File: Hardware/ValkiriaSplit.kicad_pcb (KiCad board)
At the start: 4 copper layers, 350 x 195 mm, 306 parts, among them J1 BAT, J2 TagConnect, J3 0.96_TFT_MODULE, J4 BAT, J5 TagConnect, J6 0.96_TFT_MODULE, Q1 AO3401A, Q2 AO3401A, Q3 AO3401A, Q4 AO3401A, SW1 MSK12C02, SW10 PG1350, SW11 PG1350, SW12 PG1350, SW13 PG1350, SW14 PG1350, SW15 PG1350, SW16 PG1350, SW17 PG1350, SW18 PG1350, SW19 PG1350, SW2 MSK12C02, SW20 PG1350, SW21 PG1350, SW22 PG1350, SW23 PG1350, SW24 PG1350, SW25 PG1350, SW26 PG1350, SW27 PG1350, SW28 PG1350, SW29 PG1350, SW3 PG1350, SW30 PG1350, SW31 PG1350, SW32 ENCODER, SW33 PG1350, SW34 PG1350, SW35 PG1350, SW36 PG1350, SW37 PG1350, SW38 PG1350, SW39 PG1350, SW4 PG1350, SW40 PG1350, SW41 PG1350, SW42 PG1350, SW43 PG1350, SW44 PG1350, SW45 PG1350, SW46 PG1350, SW47 PG1350, SW48 PG1350, SW49 PG1350, SW5 PG1350, SW50 PG1350, SW51 PG1350, SW52 PG1350, SW53 PG1350, SW54 PG1350, SW55 PG1350, SW56 PG1350, SW57 PG1350, SW58 PG1350, SW59 PG1350, SW6 PG1350, SW60 PG1350, SW61 PG1350, SW62 ENCODER, SW7 PG1350, SW8 PG1350, SW9 PG1350, U1 TPS61040DBV, U2 XIAO-NRF52840-PLUS, U3 TPS61040DBV, U4 XIAO-NRF52840-PLUS

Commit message: Key matrix and edges
Defined the key matrix locations and the board edges.
Next step: start routing and verify the buck converter layout.
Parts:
- added C75: 100n, Capacitor_SMD:C_0603_1608Metric, F.Cu at (259.0, 216.8)
- added C76: 100n, Capacitor_SMD:C_0603_1608Metric, F.Cu at (259.0, 219.3)
- added D125: SK6812MINI-E, Custom_Parts:LED_SK6812MINI-E_3.2x2.8mm_P1.5mm_ReverseMount, B.Cu at (313.7, 96.4)
- added D126: SK6812MINI-E, Custom_Parts:LED_SK6812MINI-E_3.2x2.8mm_P1.5mm_ReverseMount, B.Cu at (275.6, 127.3)
- added R23: 10K, Resistor_SMD:R_0603_1608Metric, F.Cu at (308.4, 230.8)
- added R24: 22, Resistor_SMD:R_0603_1608Metric, F.Cu at (308.4, 233.3)
- added R25: 0, Resistor_SMD:R_0603_1608Metric, F.Cu at (113.0, 220.9)
- added R26: 0, Resistor_SMD:R_0603_1608Metric, F.Cu at (113.0, 223.4)
- added R27: 0, Resistor_SMD:R_0603_1608Metric, F.Cu at (259.0, 221.8)
- added R28: 0, Resistor_SMD:R_0603_1608Metric, F.Cu at (259.0, 224.3)
- added SW63: PG1350, Custom_Parts:PG1350_1.00u_PCB, F.Cu at (330.2, 125.5)
- added SW64: PG1350, Custom_Parts:PG1350_1.00u_PCB, F.Cu at (330.2, 144.6)
- added SW65: PG1350, Custom_Parts:PG1350_1.00u_PCB, F.Cu at (330.2, 163.6)
- added SW66: ENCODER, Custom_Parts:ALPS_EC11J_ENCODER, F.Cu at (216.4, 134.0)
- C13, FID1, FID2, FID3, FID4: moved to B.Cu
- C42, C73, C74: value 100n -> 1u; moved to B.Cu
- C44: value 1u -> 100n; moved to F.Cu
- D103, D104, D119, D120, D17, D26, D35, D44, D47, D60, D76, D77, D85, D86, D94, D95: value SK6812MINI-E -> 1N4148WT; footprint Custom_Parts:LED_SK6812MINI-E_3.2x2.8mm_P1.5mm_ReverseMount -> Diode_SMD:D_SOD-523
- D114, D115, D12, D21, D30, D39, D52, D55, D71, D72, D80, D81, D89, D90, D98, D99: value 1N4148WT -> SK6812MINI-E; footprint Diode_SMD:D_SOD-523 -> Custom_Parts:LED_SK6812MINI-E_3.2x2.8mm_P1.5mm_ReverseMount
- J3, J6: footprint Custom_Parts:Jushuo_AFC07-S06FCA-00_1x8-1MP_P0.50_Horizontal -> Custom_Parts:0.96_TFT_MODULE; moved to B.Cu
- L1, L2: footprint Custom_Parts:VLCF4020 -> Custom_Parts:VLCF4020_MIRROR
- R1: value 500 -> 100K
- R10: value 500 -> 10K
- R11: value 100K -> 10K
- R12: value 10K -> 22
- R13: value 470K -> 100K
- R14: value 150K -> 500
- R15: value 100 -> 10K
- R16: value 10K -> 470K
- R17: value 10K -> 150K
- R18: value 22 -> 0
- R2: value 100K -> 500
- R21: value 0 -> 100
- R22: value 0 -> 10K
- R6: value 100 -> 0
- R7, R8: value 10K -> 0
- R9: value 22 -> 100
- SW2: value MSK12C02 -> RESET; footprint Custom_Parts:MSK12C02 -> Button_Switch_SMD:SW_SPST_TS-1088-xR020
- SW3: value PG1350 -> MSK12C02; footprint Custom_Parts:PG1350_1.00u_PCB -> Custom_Parts:MSK12C02
- SW32, SW62: value ENCODER -> PG1350; footprint Custom_Parts:ALPS_EC11J_ENCODER -> Custom_Parts:PG1350_1.00u_PCB
- SW35: value PG1350 -> ENCODER; footprint Custom_Parts:PG1350_1.00u_PCB -> Custom_Parts:ALPS_EC11J_ENCODER
- SW4: value PG1350 -> RESET; footprint Custom_Parts:PG1350_1.00u_PCB -> Button_Switch_SMD:SW_SPST_TS-1088-xR020
- moved R10 381.5 mm to (86.1, 231.5)
- moved R11 381.5 mm to (86.1, 234.0)
- moved R12 381.5 mm to (86.1, 236.5)
- moved SW2 332.1 mm to (145.4, 233.9)
- moved R20 316.8 mm to (288.5, 221.0)
- moved R19 316.8 mm to (288.5, 218.5)
- moved SW34 306.2 mm to (64.8, 163.6), turned to 180 degrees
- moved R16 271.0 mm to (208.5, 239.0)
- moved R17 267.2 mm to (212.0, 240.0)
- moved C9 263.4 mm to (208.5, 241.0)
- moved SW4 260.9 mm to (288.1, 234.1)
- moved D1 258.5 mm to (193.5, 234.3)
- moved R15 256.5 mm to (215.5, 240.0), turned to 180 degrees
- moved Q1 256.2 mm to (193.5, 237.8), turned to -90 degrees
- moved C44 255.1 mm to (113.0, 218.4), turned to 0 degrees
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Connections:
- net /Control_Left/VFBL renamed /Control_Left/VFB
- net /Control_Left/VSWL renamed /Control_Left/VSW
- net /Control_Right/VSWR renamed /Control_Right/VSW
- C42 pad 1: /Matrix_Left/ENC_CC -> 5VL
- C43 pad 1: /Matrix_Left/ENC_CW -> /Matrix_Left/ENC_CC
- C44 pad 1: 5VR -> /Matrix_Left/ENC_CW
- C73 pad 1: /Matrix_Right/ENC_CC -> 5VR
- C74 pad 1: /Matrix_Right/ENC_CW -> 5VR
- C9 pad 2: /Control_Right/VFBR -> /Control_Right/VFB
- D100 pad 1: ROW3_R -> ROW1_R
- D101 pad 1: ROW4_R -> ROW2_R
- D102 pad 1: ROW5_R -> ROW3_R
- D103 pad 1: GND -> ROW4_R
- D103 pad 2: Net-(D103-DIN) -> Net-(D103-A)
- D104 pad 1: GND -> ROW5_R
- D104 pad 2: Net-(D104-DIN) -> Net-(D104-A)
- D112 pad 4: Net-(D103-DIN) -> Net-(D112-DOUT)
- D113 pad 4: Net-(D104-DIN) -> Net-(D113-DOUT)
- D114 pad 1: ROW1_R -> GND
- D114 pad 2: Net-(D114-A) -> Net-(D114-DIN)
- D115 pad 1: ROW2_R -> GND
- D115 pad 2: Net-(D115-A) -> Net-(D115-DIN)
- D116 pad 1: ROW3_R -> ROW1_R
- D117 pad 1: ROW4_R -> ROW2_R
- D118 pad 1: ROW5_R -> ROW3_R
- D118 pad 2: /Matrix_Right/ENC_SW -> Net-(D118-A)
- D119 pad 1: GND -> ROW4_R
- D119 pad 2: Net-(D105-DOUT) -> Net-(D119-A)
- D12 pad 1: ROW1_L -> GND
- D12 pad 2: Net-(D12-A) -> Net-(D12-DIN)
- D120 pad 1: GND -> ROW5_R
- D120 pad 2: Net-(D106-DOUT) -> /Matrix_Right/ENC_SW
- D121 pad 2: Net-(D121-DIN) -> Net-(D112-DOUT)
- D121 pad 4: Net-(D112-DIN) -> Net-(D121-DOUT)
- D122 pad 2: Net-(D122-DIN) -> Net-(D113-DOUT)
- D122 pad 4: Net-(D113-DIN) -> Net-(D122-DOUT)
- D123 pad 2: Net-(D119-DOUT) -> Net-(D123-DIN)
- D123 pad 4: Net-(D121-DIN) -> Net-(D114-DIN)
- D124 pad 2: Net-(D120-DOUT) -> Net-(D124-DIN)
- D124 pad 4: Net-(D122-DIN) -> Net-(D115-DIN)
- D13 pad 1: ROW2_L -> ROW1_L
- D14 pad 1: ROW3_L -> ROW2_L
- D15 pad 1: ROW4_L -> ROW3_L
- D16 pad 1: ROW5_L -> ROW4_L
- D17 pad 1: GND -> ROW5_L
- D17 pad 2: Net-(D17-DIN) -> Net-(D17-A)
- D19 pad 2: Net-(D10-DOUT) -> Net-(D19-DIN)
- D19 pad 4: Net-(D19-DOUT) -> Net-(D10-DIN)
- D21 pad 1: ROW1_L -> GND
- D21 pad 2: Net-(D21-A) -> Net-(D12-DOUT)
- D22 pad 1: ROW2_L -> ROW1_L
- D23 pad 1: ROW3_L -> ROW2_L
- D24 pad 1: ROW4_L -> ROW3_L
- D25 pad 1: ROW5_L -> ROW4_L
- D26 pad 1: GND -> ROW5_L
- D26 pad 2: Net-(D26-DIN) -> Net-(D26-A)
- D28 pad 2: Net-(D19-DOUT) -> Net-(D28-DIN)
- D28 pad 4: Net-(D28-DOUT) -> Net-(D19-DIN)
- D30 pad 1: ROW1_L -> GND
- D30 pad 2: Net-(D30-A) -> Net-(D21-DOUT)
- D31 pad 1: ROW2_L -> ROW1_L
- D32 pad 1: ROW3_L -> ROW2_L
- D33 pad 1: ROW4_L -> ROW3_L
- D34 pad 1: ROW5_L -> ROW4_L
- D35 pad 1: GND -> ROW5_L
- D35 pad 2: Net-(D35-DIN) -> Net-(D35-A)
- D37 pad 2: Net-(D28-DOUT) -> Net-(D37-DIN)
- D37 pad 4: Net-(D37-DOUT) -> Net-(D28-DIN)
- D39 pad 1: ROW1_L -> GND
- D39 pad 2: Net-(D39-A) -> Net-(D30-DOUT)
- D40 pad 1: ROW2_L -> ROW1_L
- D41 pad 1: ROW3_L -> ROW2_L
- D42 pad 1: ROW4_L -> ROW3_L
- D43 pad 1: ROW5_L -> ROW4_L
- D44 pad 1: GND -> ROW5_L
- D44 pad 2: Net-(D44-DIN) -> Net-(D44-A)
- D46 pad 2: Net-(D37-DOUT) -> Net-(D46-DIN)
- D46 pad 4: Net-(D46-DOUT) -> Net-(D37-DIN)
- D47 pad 1: GND -> ROW1_L
- D47 pad 2: Net-(D38-DOUT) -> Net-(D47-A)
- D48 pad 1: ROW1_L -> ROW2_L
- D49 pad 1: ROW2_L -> ROW3_L
- D50 pad 1: ROW3_L -> ROW4_L
- D51 pad 1: ROW4_L -> ROW5_L
- D52 pad 1: ROW5_L -> GND
- D52 pad 2: Net-(D52-A) -> Net-(D38-DOUT)
- D53 pad 2: Net-(D53-DIN) -> Net-(D39-DOUT)
- D53 pad 4: Net-(D44-DIN) -> Net-(D53-DOUT)
- D55 pad 1: ROW1_L -> GND
- D55 pad 2: Net-(D55-A) -> Net-(D55-DIN)
- D56 pad 1: ROW2_L -> ROW1_L
- D57 pad 1: ROW3_L -> ROW2_L
- D58 pad 1: ROW4_L -> ROW3_L
- D59 pad 1: ROW5_L -> ROW4_L
- D59 pad 2: /Matrix_Left/ENC_SW -> Net-(D59-A)
- D6 pad 1: 3V3L -> 3V3R
- D60 pad 1: GND -> ROW5_L
- D60 pad 2: Net-(D46-DOUT) -> /Matrix_Left/ENC_SW
- D61 pad 2: Net-(D47-DOUT) -> Net-(D52-DOUT)
- D62 pad 2: Net-(D62-DIN) -> Net-(D53-DOUT)
- D62 pad 4: Net-(D53-DIN) -> Net-(D62-DOUT)
- D64 pad 2: Net-(D60-DOUT) -> Net-(D64-DIN)
- D64 pad 4: Net-(D62-DIN) -> Net-(D55-DIN)
- D66 pad 2: LED_DATA_R -> Net-(D62-DOUT)
- D66 pad 3: 5VR -> 5VL
- D66 pad 4: Net-(D66-DOUT) -> Net-(D64-DIN)
- D67 pad 4: Net-(D67-DOUT) -> unconnected-(D67-DOUT-Pad4)
- D68 pad 2: Net-(D68-DIN) -> LED_DATA_R
- D68 pad 4: unconnected-(D68-DOUT-Pad4) -> Net-(D68-DOUT)
- D69 pad 2: Net-(D66-DOUT) -> Net-(D69-DIN)
- D7 pad 2: LED_DATA_L -> Net-(D10-DOUT)
- D7 pad 4: Net-(D10-DIN) -> unconnected-(D7-DOUT-Pad4)
- D70 pad 2: Net-(D67-DOUT) -> Net-(D70-DIN)
- D70 pad 4: Net-(D70-DOUT) -> Net-(D67-DIN)
- D71 pad 1: ROW1_R -> GND
- D71 pad 2: Net-(D71-A) -> Net-(D68-DOUT)
- D72 pad 1: ROW2_R -> GND
- D72 pad 2: Net-(D72-A) -> Net-(D69-DOUT)
- D73 pad 1: ROW3_R -> ROW1_R
- D74 pad 1: ROW4_R -> ROW2_R
- D75 pad 1: ROW5_R -> ROW3_R
- D76 pad 1: GND -> ROW4_R
- D76 pad 2: Net-(D76-DIN) -> Net-(D76-A)
- D77 pad 1: GND -> ROW5_R
- D77 pad 2: Net-(D77-DIN) -> Net-(D77-A)
- D78 pad 2: Net-(D69-DOUT) -> Net-(D78-DIN)
- D78 pad 4: Net-(D78-DOUT) -> Net-(D69-DIN)
- D79 pad 2: Net-(D70-DOUT) -> Net-(D79-DIN)
- D79 pad 4: Net-(D79-DOUT) -> Net-(D70-DIN)
- D8 pad 2: Net-(D17-DOUT) -> LED_DATA_L
- D80 pad 1: ROW1_R -> GND
- D80 pad 2: Net-(D80-A) -> Net-(D71-DOUT)
- D81 pad 1: ROW2_R -> GND
- D81 pad 2: Net-(D81-A) -> Net-(D72-DOUT)
- D82 pad 1: ROW3_R -> ROW1_R
- D83 pad 1: ROW4_R -> ROW2_R
- D84 pad 1: ROW5_R -> ROW3_R
- D85 pad 1: GND -> ROW4_R
- D85 pad 2: Net-(D85-DIN) -> Net-(D85-A)
- D86 pad 1: GND -> ROW5_R
- D86 pad 2: Net-(D86-DIN) -> Net-(D86-A)
- D87 pad 2: Net-(D78-DOUT) -> Net-(D87-DIN)
- D87 pad 4: Net-(D87-DOUT) -> Net-(D78-DIN)
- D88 pad 2: Net-(D79-DOUT) -> Net-(D88-DIN)
- D88 pad 4: Net-(D88-DOUT) -> Net-(D79-DIN)
- D89 pad 1: ROW1_R -> GND
- D89 pad 2: Net-(D89-A) -> Net-(D80-DOUT)
- D9 pad 4: unconnected-(D9-DOUT-Pad4) -> Net-(D12-DIN)
- D90 pad 1: ROW2_R -> GND
- D90 pad 2: Net-(D90-A) -> Net-(D81-DOUT)
- D91 pad 1: ROW3_R -> ROW1_R
- D92 pad 1: ROW4_R -> ROW2_R
- D93 pad 1: ROW5_R -> ROW3_R
- D94 pad 1: GND -> ROW4_R
- D94 pad 2: Net-(D103-DOUT) -> Net-(D94-A)
- D95 pad 1: GND -> ROW5_R
- D95 pad 2: Net-(D104-DOUT) -> Net-(D95-A)
- D96 pad 2: Net-(D87-DOUT) -> Net-(D105-DOUT)
- D96 pad 4: Net-(D105-DIN) -> Net-(D87-DIN)
- D97 pad 2: Net-(D88-DOUT) -> Net-(D106-DOUT)
- D97 pad 4: Net-(D106-DIN) -> Net-(D88-DIN)
- D98 pad 1: ROW1_R -> GND
- D98 pad 2: Net-(D98-A) -> Net-(D89-DOUT)
- D99 pad 1: ROW2_R -> GND
- D99 pad 2: Net-(D99-A) -> Net-(D90-DOUT)
- R1 pad 1: /Control_Left/LED_DATA -> VBUSL
- R1 pad 2: LED_DATA_L -> GND
- R10 pad 1: /Control_Right/LED_DATA -> 3V3L
- R10 pad 2: LED_DATA_R -> /Control_Left/LCD_RES
- R11 pad 1: VBUSR -> /Control_Left/BKLD
- R11 pad 2: GND -> /Control_Left/BKLG
- R12 pad 1: GND -> /Control_Left/BKLD
- R12 pad 2: /Control_Right/LED_EN -> /Control_Left/BKL
- R13 pad 1: 5VR -> VBUSR
- R13 pad 2: /Control_Right/VFBR -> GND
- R14 pad 1: /Control_Right/VFBR -> /Control_Right/LED_DATA
- R14 pad 2: GND -> LED_DATA_R
- R15 pad 1: /Control_Right/LCD_BKL -> GND
- R15 pad 2: /Control_Right/BKLG -> /Control_Right/LED_EN
- R16 pad 1: 3V3L -> 5VR
- R16 pad 2: /Control_Right/LCD_RES -> /Control_Right/VFB
- R17 pad 1: /Control_Right/BKLD -> /Control_Right/VFB
- R17 pad 2: /Control_Right/BKLG -> GND
- R18 pad 1: /Control_Right/BKLD -> Net-(U4-P1.15_MOSI)
- R18 pad 2: /Control_Right/BKL -> /Control_Right/LCD_MOSI
- R19 pad 1: ENC_CW_L -> Net-(U4-P1.14_MISO)
- R19 pad 2: /Matrix_Left/ENC_CW -> /Control_Right/LCD_DC
- R2 pad 1: VBUSL -> /Control_Left/LED_DATA
- R2 pad 2: GND -> LED_DATA_L
- R20 pad 1: ENC_CC_L -> Net-(U4-P1.13_SCK)
- R20 pad 2: /Matrix_Left/ENC_CC -> /Control_Right/LCD_SCK
- R21 pad 1: ENC_CW_R -> /Control_Right/LCD_BKL
- R21 pad 2: /Matrix_Right/ENC_CW -> /Control_Right/BKLG
- R22 pad 1: ENC_CC_R -> 3V3R
- R22 pad 2: /Matrix_Right/ENC_CC -> /Control_Right/LCD_RES
- R6 pad 1: /Control_Left/LCD_BKL -> Net-(U2-P1.15_MOSI)
- R6 pad 2: /Control_Left/BKLG -> /Control_Left/LCD_MOSI
- R7 pad 1: 3V3L -> Net-(U2-P1.14_MISO)
- R7 pad 2: /Control_Left/LCD_RES -> /Control_Left/LCD_DC
- R8 pad 1: /Control_Left/BKLD -> Net-(U2-P1.13_SCK)
- R8 pad 2: /Control_Left/BKLG -> /Control_Left/LCD_SCK
- R9 pad 1: /Control_Left/BKLD -> /Control_Left/LCD_BKL
- R9 pad 2: /Control_Left/BKL -> /Control_Left/BKLG
- SW10 pad 2: Net-(D23-A) -> Net-(D22-A)
- SW11 pad 2: Net-(D24-A) -> Net-(D23-A)
- SW12 pad 2: Net-(D25-A) -> Net-(D24-A)
- SW13 pad 1: COL3_L -> COL2_L
- SW13 pad 2: Net-(D30-A) -> Net-(D25-A)
- SW14 pad 1: COL3_L -> COL2_L
- SW14 pad 2: Net-(D31-A) -> Net-(D26-A)
- SW15 pad 2: Net-(D32-A) -> Net-(D31-A)
- SW16 pad 2: Net-(D33-A) -> Net-(D32-A)
- SW17 pad 2: Net-(D34-A) -> Net-(D33-A)
- SW18 pad 1: COL4_L -> COL3_L
- SW18 pad 2: Net-(D39-A) -> Net-(D34-A)
- SW19 pad 1: COL4_L -> COL3_L
- SW19 pad 2: Net-(D40-A) -> Net-(D35-A)
- SW2 pad 1: unconnected-(SW2-A-Pad1) -> /Control_Left/~{RESET}
- SW2 pad 2: /Control_Right/VBAT -> GND
- SW20 pad 2: Net-(D41-A) -> Net-(D40-A)
- SW21 pad 2: Net-(D42-A) -> Net-(D41-A)
- SW22 pad 2: Net-(D43-A) -> Net-(D42-A)
- SW23 pad 1: COL5_L -> COL4_L
- SW23 pad 2: Net-(D48-A) -> Net-(D43-A)
- SW24 pad 1: COL5_L -> COL4_L
- SW24 pad 2: Net-(D49-A) -> Net-(D44-A)
- SW25 pad 2: Net-(D50-A) -> Net-(D47-A)
- SW26 pad 2: Net-(D51-A) -> Net-(D48-A)
- SW27 pad 2: Net-(D52-A) -> Net-(D49-A)
- SW28 pad 1: COL6_L -> COL5_L
- SW28 pad 2: Net-(D55-A) -> Net-(D50-A)
- SW29 pad 1: COL6_L -> COL5_L
- SW29 pad 2: Net-(D56-A) -> Net-(D51-A)
- SW3 pad 1: COL1_L -> unconnected-(SW3-A-Pad1)
- SW3 pad 2: Net-(D12-A) -> /Control_Right/VBAT
- SW30 pad 2: Net-(D57-A) -> Net-(D56-A)
- SW31 pad 2: Net-(D58-A) -> Net-(D57-A)
- SW33 pad 1: COL1_R -> COL6_L
- SW33 pad 2: Net-(D71-A) -> Net-(D59-A)
- SW34 pad 1: COL1_R -> COL6_L
- SW34 pad 2: Net-(D72-A) -> /Matrix_Left/ENC_SW
- SW36 pad 2: Net-(D74-A) -> Net-(D73-A)
- SW37 pad 2: Net-(D75-A) -> Net-(D74-A)
- SW38 pad 1: COL2_R -> COL1_R
- SW38 pad 2: Net-(D80-A) -> Net-(D75-A)
- SW39 pad 1: COL2_R -> COL1_R
- SW39 pad 2: Net-(D81-A) -> Net-(D76-A)
- SW4 pad 1: COL1_L -> /Control_Right/~{RESET}
- SW4 pad 2: Net-(D13-A) -> GND
- SW40 pad 1: COL2_R -> COL1_R
- SW40 pad 2: Net-(D82-A) -> Net-(D77-A)
- SW41 pad 2: Net-(D83-A) -> Net-(D82-A)
- SW42 pad 2: Net-(D84-A) -> Net-(D83-A)
- SW43 pad 1: COL3_R -> COL2_R
- SW43 pad 2: Net-(D89-A) -> Net-(D84-A)
- SW44 pad 1: COL3_R -> COL2_R
- SW44 pad 2: Net-(D90-A) -> Net-(D85-A)
- SW45 pad 1: COL3_R -> COL2_R
- SW45 pad 2: Net-(D91-A) -> Net-(D86-A)
- SW46 pad 2: Net-(D92-A) -> Net-(D91-A)
- SW47 pad 2: Net-(D93-A) -> Net-(D92-A)
- SW48 pad 1: COL4_R -> COL3_R
- SW48 pad 2: Net-(D98-A) -> Net-(D93-A)
- SW49 pad 1: COL4_R -> COL3_R
- SW49 pad 2: Net-(D99-A) -> Net-(D94-A)
- SW5 pad 2: Net-(D14-A) -> Net-(D13-A)
- SW50 pad 1: COL4_R -> COL3_R
- SW50 pad 2: Net-(D100-A) -> Net-(D95-A)
- SW51 pad 2: Net-(D101-A) -> Net-(D100-A)
- SW52 pad 2: Net-(D102-A) -> Net-(D101-A)
- SW53 pad 1: COL5_R -> COL4_R
- SW53 pad 2: Net-(D107-A) -> Net-(D102-A)
- SW54 pad 1: COL5_R -> COL4_R
- SW54 pad 2: Net-(D108-A) -> Net-(D103-A)
- SW55 pad 1: COL5_R -> COL4_R
- SW55 pad 2: Net-(D109-A) -> Net-(D104-A)
- SW56 pad 2: Net-(D110-A) -> Net-(D107-A)
- SW57 pad 2: Net-(D111-A) -> Net-(D108-A)
- SW58 pad 1: COL6_R -> COL5_R
- SW58 pad 2: Net-(D114-A) -> Net-(D109-A)
- SW59 pad 1: COL6_R -> COL5_R
- SW59 pad 2: Net-(D115-A) -> Net-(D110-A)
- SW6 pad 2: Net-(D15-A) -> Net-(D14-A)
- SW60 pad 1: COL6_R -> COL5_R
- SW60 pad 2: Net-(D116-A) -> Net-(D111-A)
- SW61 pad 2: Net-(D117-A) -> Net-(D116-A)
- SW7 pad 2: Net-(D16-A) -> Net-(D15-A)
- SW8 pad 1: COL2_L -> COL1_L
- SW8 pad 2: Net-(D21-A) -> Net-(D16-A)
- SW9 pad 1: COL2_L -> COL1_L
- SW9 pad 2: Net-(D22-A) -> Net-(D17-A)
- U2 pad 10: /Control_Left/LCD_DC -> Net-(U2-P1.14_MISO)
- U2 pad 11: /Control_Left/LCD_MOSI -> Net-(U2-P1.15_MOSI)
- U2 pad 19: ENC_CW_L -> ENC_CC_L
- U2 pad 20: ENC_CC_L -> ENC_CW_L
- U2 pad 9: /Control_Left/LCD_SCK -> Net-(U2-P1.13_SCK)
- U3 pad 3: /Control_Right/VFBR -> /Control_Right/VFB
- U4 pad 10: /Control_Right/LCD_DC -> Net-(U4-P1.14_MISO)
- U4 pad 11: /Control_Right/LCD_MOSI -> Net-(U4-P1.15_MOSI)
- U4 pad 19: ENC_CW_R -> ENC_CC_R
- U4 pad 20: ENC_CC_R -> ENC_CW_R
- U4 pad 9: /Control_Right/LCD_SCK -> Net-(U4-P1.13_SCK)
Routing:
- net /Control_Left/LED_EN: track 0.00 -> 2.07 mm
- net /Control_Right/LED_EN: track 0.00 -> 2.07 mm
- added copper zone on F.Cu, net /Control_Left/VFB
- added copper zone on F.Cu, net /Control_Left/VSW
- added copper zone on F.Cu, net /Control_Right/VFB
- added copper zone on F.Cu, net /Control_Right/VSW
- added copper zone on F.Cu, net VREGL
- added copper zone on F.Cu, net VREGR
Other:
- board size 350 x 195 mm -> 284.5 x 111.4 mm
- copper layers 4 -> 2

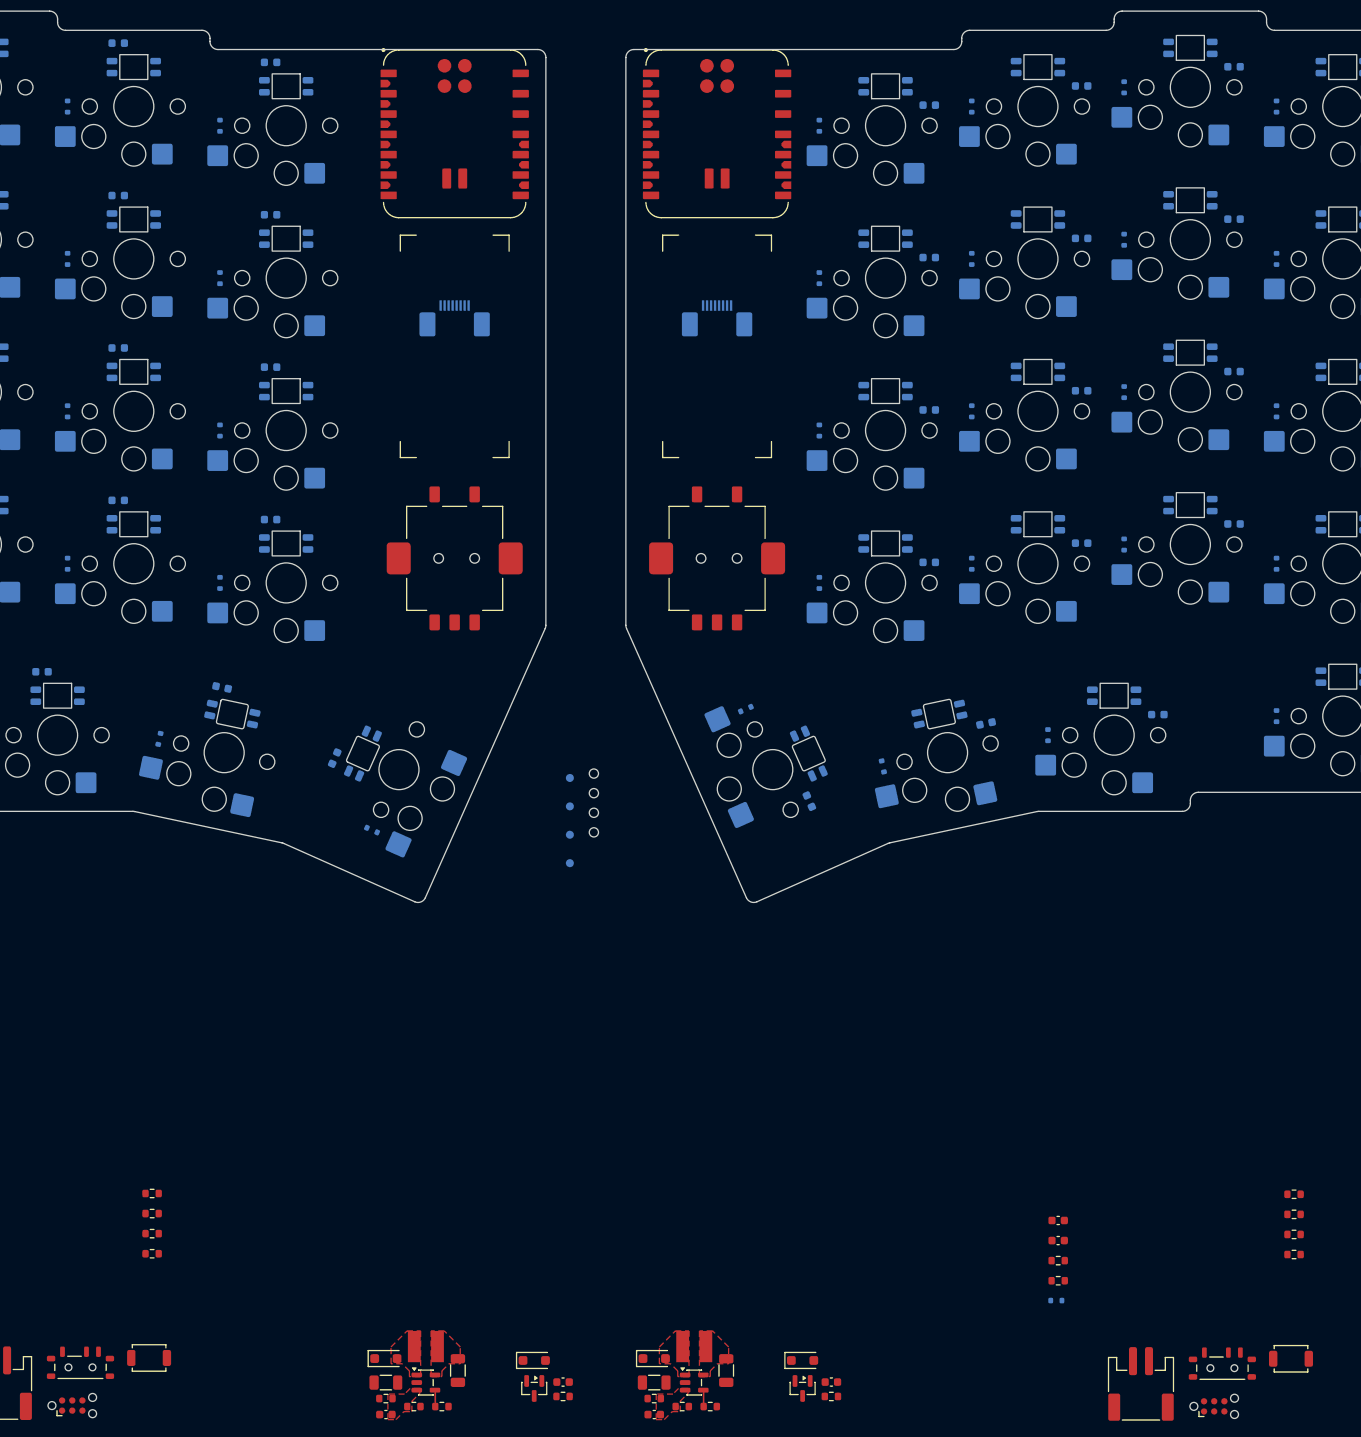
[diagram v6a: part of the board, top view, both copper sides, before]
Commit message: Pinout and footprints
Updated the MCU footprints because the silkscreen was too close to the edge.
Updated the pinout for the MCUs. The left side seems to be ok, but the right side may need some adjustments.
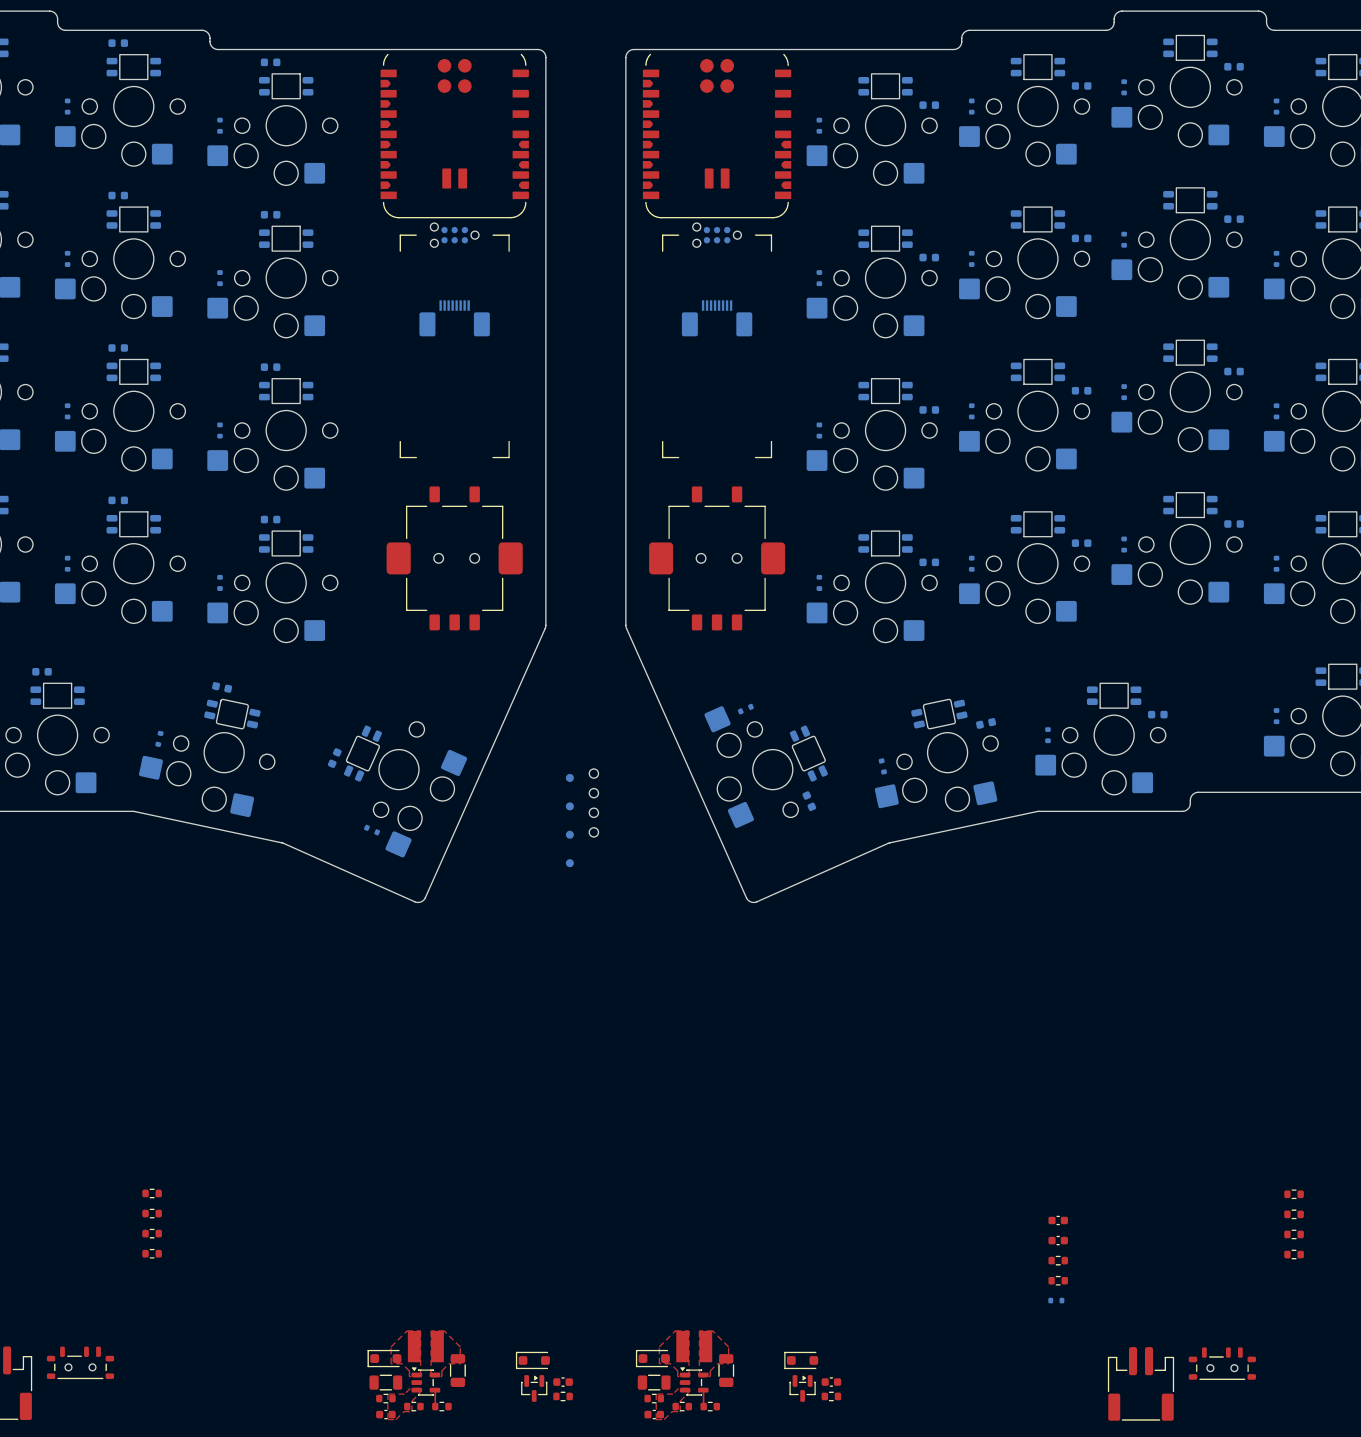
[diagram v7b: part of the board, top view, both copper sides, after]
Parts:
- removed SW2, SW4: RESET, Button_Switch_SMD:SW_SPST_TS-1088-xR020
- J2, J5: moved to B.Cu
- U2, U4: footprint Custom_Parts:XIAO-NRF52840-PLUS-SMD -> Custom_Parts:XIAO-NRF52840-PLUS-SMD-EDGE
- moved J5 159.0 mm to (216.4, 93.6), turned to 180 degrees
- moved J2 153.9 mm to (183.6, 93.6), turned to 180 degrees
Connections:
- D120 pad 2: /Matrix_Right/ENC_SW -> Net-(D120-A)
- D60 pad 2: /Matrix_Left/ENC_SW -> Net-(D60-A)
- J2 pad 3: /Control_Left/~{RESET} -> ENC_SW_R
- J5 pad 3: /Control_Right/~{RESET} -> ENC_SW_R
- SW34 pad 2: /Matrix_Left/ENC_SW -> Net-(D60-A)
- SW35 pad S1: COL6_L -> ENC_SW_R
- SW35 pad S2: /Matrix_Left/ENC_SW -> GND
- SW65 pad 2: /Matrix_Right/ENC_SW -> Net-(D120-A)
- SW66 pad S1: COL6_R -> ENC_SW_R
- SW66 pad S2: /Matrix_Right/ENC_SW -> GND
- U2 pad 1: COL1_L -> /Control_Left/LED_DATA
- U2 pad 15: /Control_Left/LCD_CS -> COL1_L
- U2 pad 16: ROW1_L -> COL2_L
- U2 pad 17: ROW2_L -> COL3_L
- U2 pad 18: ROW3_L -> COL4_L
- U2 pad 19: ENC_CC_L -> COL5_L
- U2 pad 2: COL2_L -> ROW1_L
- U2 pad 20: ENC_CW_L -> COL6_L
- U2 pad 21: /Control_Left/LCD_BKL -> ENC_CC_L
- U2 pad 22: ROW5_L -> /Control_Left/LCD_BKL
- U2 pad 23: ROW4_L -> /Control_Left/LED_EN
- U2 pad 26: /Control_Left/~{RESET} -> ENC_SW_R
- U2 pad 3: COL3_L -> ROW2_L
- U2 pad 4: COL4_L -> ROW3_L
- U2 pad 5: COL5_L -> ROW4_L
- U2 pad 6: COL6_L -> ROW5_L
- U2 pad 7: /Control_Left/LED_EN -> /Control_Left/LCD_CS
- U2 pad 8: /Control_Left/LED_DATA -> ENC_CW_L
- U4 pad 1: COL1_R -> /Control_Right/LED_DATA
- U4 pad 15: /Control_Right/LCD_CS -> COL1_R
- U4 pad 16: ROW1_R -> COL2_R
- U4 pad 17: ROW2_R -> COL3_R
- U4 pad 18: ROW3_R -> COL4_R
- U4 pad 19: ENC_CC_R -> COL5_R
- U4 pad 2: COL2_R -> ROW1_R
- U4 pad 20: ENC_CW_R -> COL6_R
- U4 pad 21: /Control_Right/LCD_BKL -> ENC_CC_R
- U4 pad 22: ROW5_R -> /Control_Right/LCD_BKL
- U4 pad 23: ROW4_R -> /Control_Right/LED_EN
- U4 pad 26: /Control_Right/~{RESET} -> ENC_SW_R
- U4 pad 3: COL3_R -> ROW2_R
- U4 pad 4: COL4_R -> ROW3_R
- U4 pad 5: COL5_R -> ROW4_R
- U4 pad 6: COL6_R -> ROW5_R
- U4 pad 7: /Control_Right/LED_EN -> /Control_Right/LCD_CS
- U4 pad 8: /Control_Right/LED_DATA -> ENC_CW_R

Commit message: Reset button and LED switch
Added an LED power switch.
Returned the reset button for bootloader access.
Focus on changing the display to an e-ink one for lower power consumption.
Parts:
- removed the R13 at (230.7, 238.8)
- removed the R16 at (208.5, 239.0)
- removed the R17 at (212.0, 240.0)
- removed the R3 at (182.0, 240.0)
- removed the U3 at (213.5, 237.0)
- added R12: 100K, Resistor_SMD:R_0603_1608Metric, F.Cu at (230.7, 238.8)
- added R14: 470K, Resistor_SMD:R_0603_1608Metric, F.Cu at (208.5, 239.0)
- added SW2: SW_Push, Button_Switch_SMD:SW_SPST_TS-1088-xR020, F.Cu at (68.0, 232.9)
- added SW3: MSK12C02, Custom_Parts:MSK12C02, F.Cu at (69.5, 228.4)
- added SW5: SW_Push, Button_Switch_SMD:SW_SPST_TS-1088-xR020, F.Cu at (330.8, 229.5)
- added SW6: MSK12C02, Custom_Parts:MSK12C02, F.Cu at (332.3, 225.0)
- added U4: TPS61040DBV, Package_TO_SOT_SMD:SOT-23-5, F.Cu at (213.5, 237.0)
- R15: value 10K -> 150K
- moved R15 3.50 mm to (212.0, 240.0), turned to 0 degrees
- renumbered R11 to R10, R12 to R11, R14 to R13, R18 to R16, R19 to R17, R20 to R18, R21 to R19, R22 to R20, R23 to R21, R24 to R22, R25 to R23, R26 to R24, R27 to R25, R28 to R26, R4 to R3, R5 to R4, R6 to R5, R7 to R6, R8 to R7, R9 to R8, R10 to R9, SW8 to SW10, SW9 to SW11, SW10 to SW12, SW11 to SW13, SW12 to SW14, SW13 to SW15, SW14 to SW16, SW15 to SW17, SW16 to SW18, SW17 to SW19, SW18 to SW20, SW19 to SW21, SW20 to SW22, SW21 to SW23, SW22 to SW24, SW23 to SW25, SW24 to SW26, SW25 to SW27, SW26 to SW28, SW27 to SW29, SW28 to SW30, SW29 to SW31, SW30 to SW32, SW31 to SW33, SW32 to SW34, SW33 to SW35, SW34 to SW36, SW35 to SW37, SW36 to SW38, SW37 to SW39, SW3 to SW4, SW38 to SW40, SW39 to SW41, SW40 to SW42, SW41 to SW43, SW42 to SW44, SW43 to SW45, SW44 to SW46, SW45 to SW47, SW46 to SW48, SW47 to SW49, SW48 to SW50, SW49 to SW51, SW50 to SW52, SW51 to SW53, SW52 to SW54, SW53 to SW55, SW54 to SW56, SW55 to SW57, SW56 to SW58, SW57 to SW59, SW58 to SW60, SW59 to SW61, SW60 to SW62, SW61 to SW63, SW62 to SW64, SW63 to SW65, SW64 to SW66, SW65 to SW67, SW66 to SW68, SW5 to SW7, SW6 to SW8, SW7 to SW9, U2 to U1, U1 to U2, U4 to U3
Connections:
- D1 pad 1: VREGL -> /Control_Left/VCOM
- D4 pad 1: VREGR -> /Control_Right/VCOM
- J2 pad 3: ENC_SW_R -> /Control_Left/~{RESET}
- J5 pad 3: ENC_SW_R -> /Control_Right/~{RESET}
- Q1 pad 2: VREGL -> /Control_Left/VCOM
- Q3 pad 2: VREGR -> /Control_Right/VCOM
- R15 pad 1: GND -> /Control_Right/VFB
- R15 pad 2: /Control_Right/LED_EN -> GND
- U1 pad 23: /Control_Left/LED_EN -> ENC_SW_R
- U1 pad 26: ENC_SW_R -> /Control_Left/~{RESET}
- U2 pad 4: /Control_Left/LED_EN -> VREGL
- U3 pad 23: /Control_Right/LED_EN -> ENC_SW_R
- U3 pad 26: ENC_SW_R -> /Control_Right/~{RESET}
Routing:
- net /Control_Left/LED_EN: track 2.07 -> 0.00 mm
- net /Control_Right/LED_EN: track 2.07 -> 0.00 mm
